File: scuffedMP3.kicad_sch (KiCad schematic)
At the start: 10 parts, among them J1 OLED, J2 Micro_SD_Card, J3 AudioJack3, U1 ESP32-WROVER-E, U2 TP4056-42-ESOP8, U3 CP2102N-Axx-xQFN24, U4 MCP1825S, U5 PCM5102A

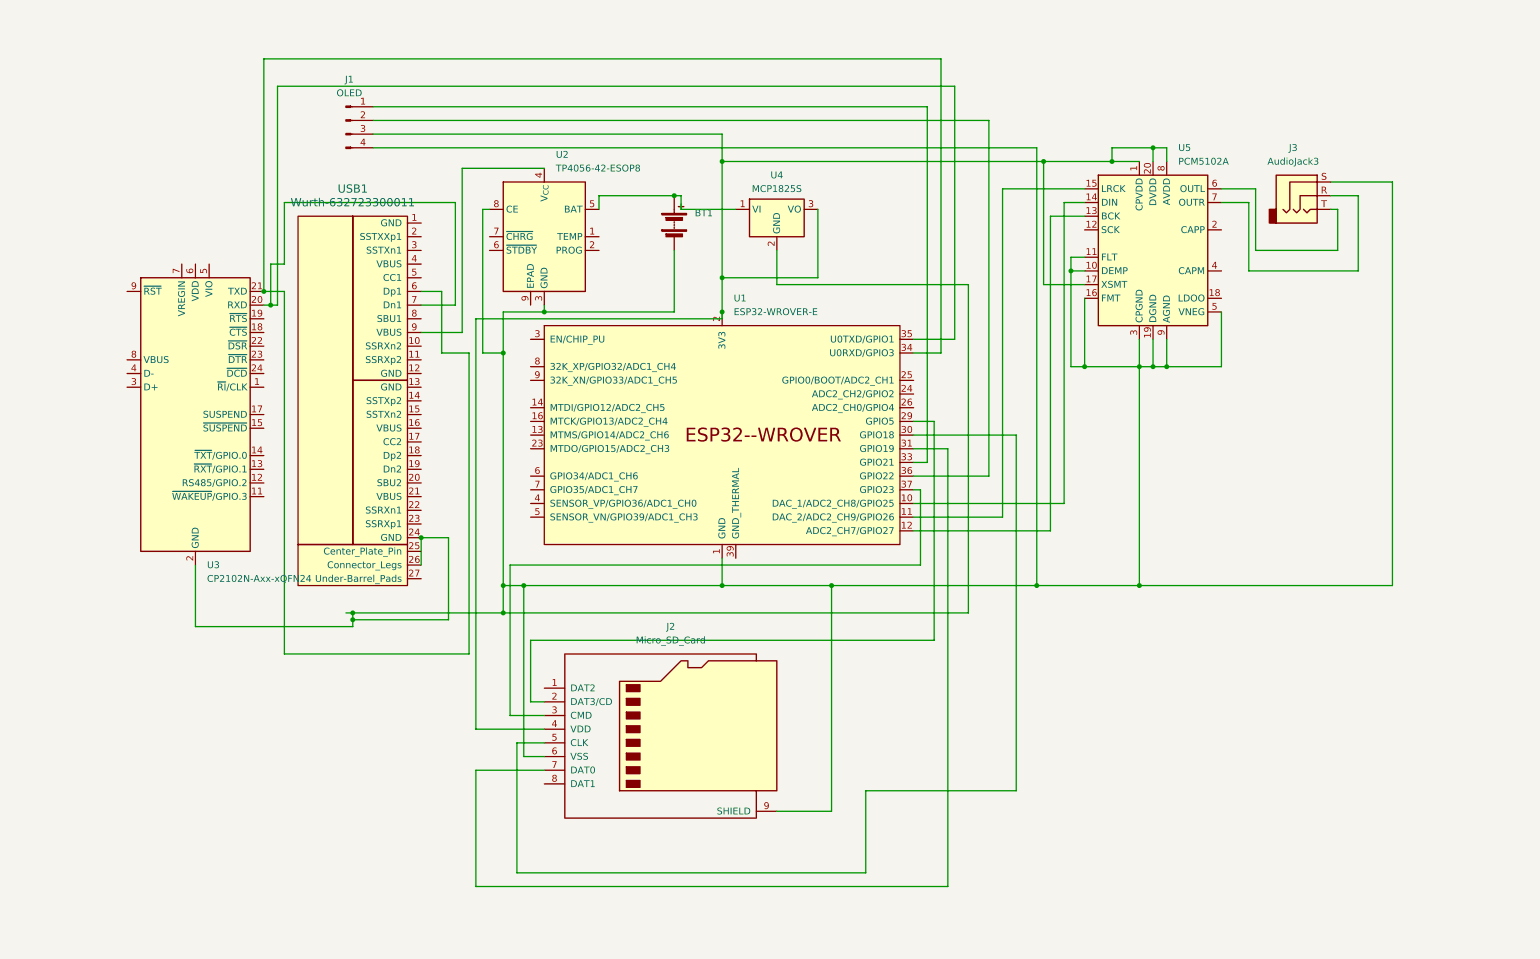
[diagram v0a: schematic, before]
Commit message: add touch sensor and wheel
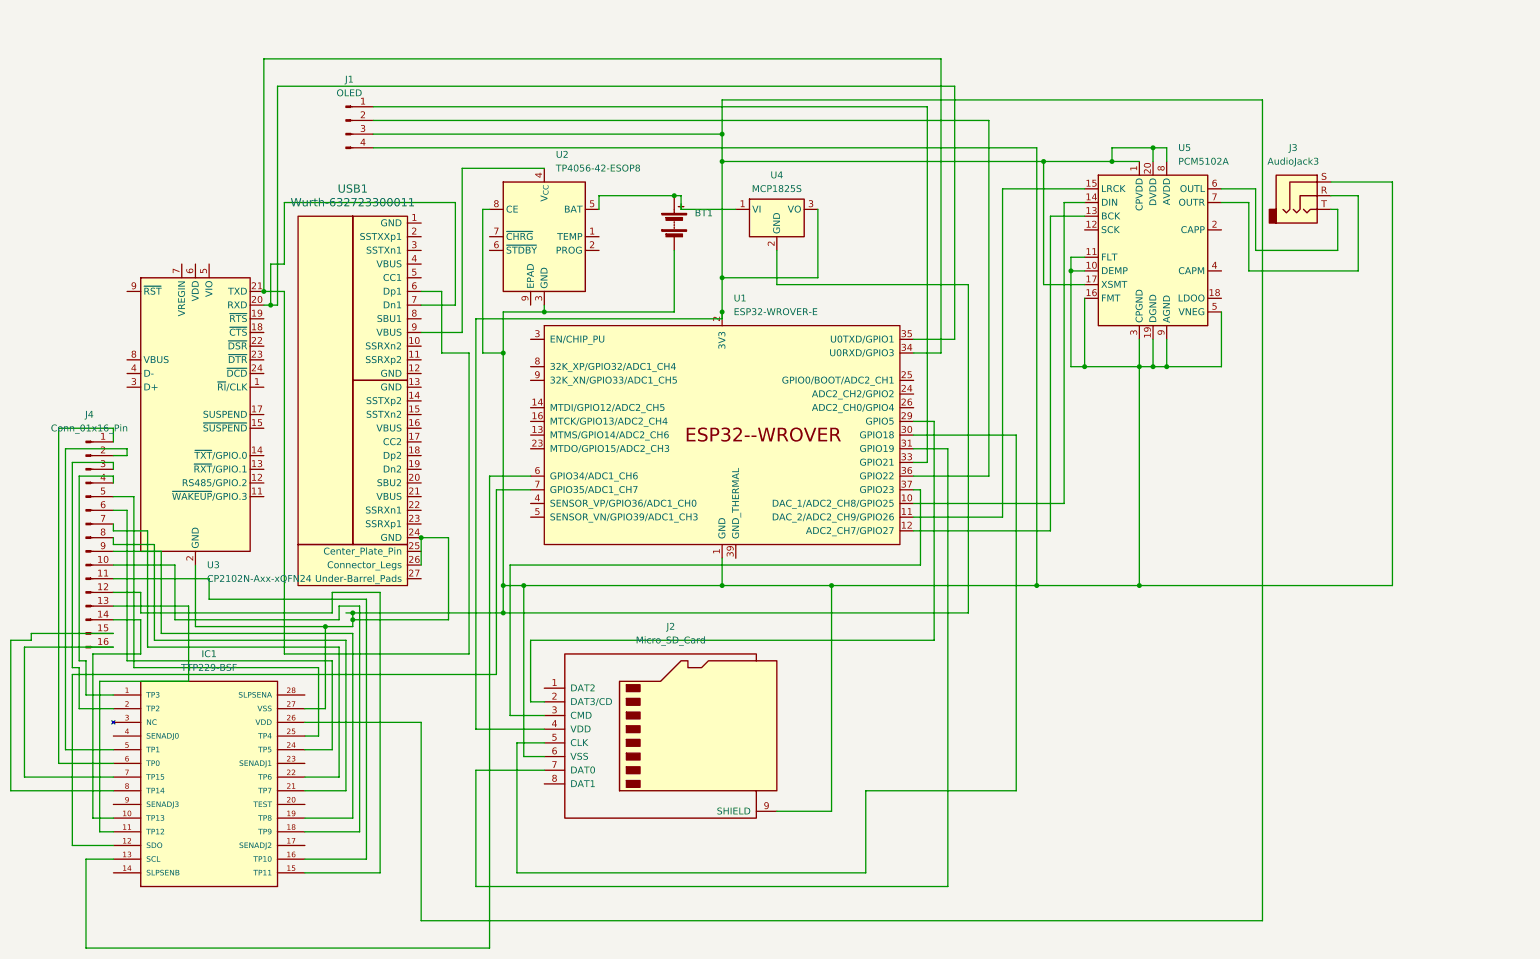
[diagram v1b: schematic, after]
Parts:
- added IC1: TTP229-BSF, TTP229-BSF:SOP64P600X175-28N, symbol TTP229-BSF:TTP229-BSF
- added J4: Conn_01x16_Pin, Library:ScrollWheel-40x12mm, symbol Connector:Conn_01x16_Pin
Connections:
- net at BT1.2 (-), J1.4 (Pin_4), J2.6 (VSS)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: now also IC1.27 (VSS)
- net at J1.3 (Pin_3), J2.4 (VDD), U1.2 (3V3)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: now also IC1.26 (VDD)
- net at U1.6 (GPIO34/ADC1_CH6): now also IC1.13 (SCL)
- net at U1.7 (GPIO35/ADC1_CH7): now also IC1.12 (SDO)
- new net: IC1.6 (TP0), J4.1 (Pin_1)
- new net: IC1.18 (TP9), J4.10 (Pin_10)
- new net: IC1.16 (TP10), J4.11 (Pin_11)
- new net: IC1.15 (TP11), J4.12 (Pin_12)
- new net: IC1.11 (TP12), J4.13 (Pin_13)
- new net: IC1.10 (TP13), J4.14 (Pin_14)
- new net: IC1.8 (TP14), J4.15 (Pin_15)
- new net: IC1.7 (TP15), J4.16 (Pin_16)
- new net: IC1.5 (TP1), J4.2 (Pin_2)
- new net: IC1.2 (TP2), J4.3 (Pin_3)
- new net: IC1.1 (TP3), J4.4 (Pin_4)
- new net: IC1.25 (TP4), J4.5 (Pin_5)
- new net: IC1.24 (TP5), J4.6 (Pin_6)
- new net: IC1.22 (TP6), J4.7 (Pin_7)
- new net: IC1.21 (TP7), J4.8 (Pin_8)
- new net: IC1.19 (TP8), J4.9 (Pin_9)

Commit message: progress
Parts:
- removed BT1: Battery, Connector_JST:JST_PH_S2B-PH-K_1x02_P2.00mm_Horizontal, symbol Device:Battery
- removed J1: OLED, OLED:128x64OLED, symbol Connector:Conn_01x04_Pin
- removed J2: Micro_SD_Card, Connector_Card:SD_Card_Device_16mm_SlotDepth, symbol Connector:Micro_SD_Card
- added 10kΩ1: R, symbol Device:R
- added C1, C3: 1 µF, Capacitor_SMD:C_0603_1608Metric, symbol Device:C_Small_US
- added C10, C8, C9: 1 µF, symbol Device:C_Small_US
- added C11: 0.1uF, symbol Device:C_Small_US
- added C2, C4: 0.1 µF, symbol Device:C_Small_US
- added C5, C6, C7: 0.1µF, symbol Device:C_Small_US
- added J2: DM3AT-SF-PEJM5, DM3AT-SF-PEJM5:HRS_DM3AT-SF-PEJM5, symbol DM3AT-SF-PEJM5:DM3AT-SF-PEJM5
- added R1: 10kΩ, symbol Device:R
- added U6: HS24S010B, easyeda2kicad:LCD-TH_L72.3-W43.0_HS24S010B, symbol OLED:HS24S010B
- J4: footprint Library:ScrollWheel-40x12mm -> Wheel:ScrollWheel-40x20mm
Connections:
- net GND: now reaches J3.S, U1.1 (GND), U1.15 (GND), U1.38 (GND), U2.3 (GND), U3.2 (GND), U3.25 (GND), U4.2 (GND), U5.16 (FMT), U5.19 (DGND), U5.3 (CPGND), U5.9 (AGND)
- net GND: now also U5.17 (XSMT), C1.2, C10.2, C11.1, C3.2, C5.1, C6.1, C7.1, C8.2, C9.2, U6.1 (GND); no longer IC1.27 (VSS), U2.8 (CE), U5.10 (DEMP), U5.11 (FLT), U5.5 (VNEG), USB1.24 (GND), USB1.26 (Connector_Legs)
- net at USB1.9 (VBUS): no longer U2.4 (V_{CC})
- net at J4.1 (Pin_1): no longer IC1.6 (TP0)
- net at J4.10 (Pin_10): no longer IC1.18 (TP9)
- net at J4.11 (Pin_11): no longer IC1.16 (TP10)
- net at J4.12 (Pin_12): no longer IC1.15 (TP11)
- net at J4.13 (Pin_13): no longer IC1.11 (TP12)
- net at J4.14 (Pin_14): no longer IC1.10 (TP13)
- net at J4.15 (Pin_15): no longer IC1.8 (TP14)
- net at J4.16 (Pin_16): no longer IC1.7 (TP15)
- net at J4.2 (Pin_2): no longer IC1.5 (TP1)
- net at J4.3 (Pin_3): no longer IC1.2 (TP2)
- net at J4.4 (Pin_4): no longer IC1.1 (TP3)
- net at J4.5 (Pin_5): no longer IC1.25 (TP4)
- net at J4.6 (Pin_6): no longer IC1.24 (TP5)
- net at J4.7 (Pin_7): no longer IC1.22 (TP6)
- net at J4.8 (Pin_8): no longer IC1.21 (TP7)
- net at J4.9 (Pin_9): no longer IC1.19 (TP8)
- net DAC DIN: now reaches U5.14 (DIN)
- net DAC DIN: now also U1.36 (GPIO22); no longer U1.10 (DAC_1/ADC2_CH8/GPIO25)
- net Bit Clock: now reaches U1.11 (DAC_2/ADC2_CH9/GPIO26)
- net Bit Clock: now also U5.13 (BCK); no longer U5.15 (LRCK)
- net OLED DC: now reaches U1.12 (ADC2_CH7/GPIO27)
- net OLED DC: now also U6.6 (DC); no longer U5.13 (BCK)
- net +3V3: now reaches U1.2 (3V3), U4.3 (VO), U5.1 (CPVDD), U5.20 (DVDD), U5.8 (AVDD)
- net +3V3: now also U3.6 (VDD), 10kΩ1.2, C1.1, C11.2, C5.2, C6.2, C7.2, R1.1, U6.2 (VCC); no longer IC1.26 (VDD), U5.17 (XSMT)
- net BOOT_SEL: now reaches U1.25 (GPIO0/BOOT/ADC2_CH1)
- net BOOT_SEL: now also 10kΩ1.1, C4.2
- net OLED CS: now reaches U1.29 (GPIO5)
- net OLED CS: now also U6.7 (CS)
- net EN: now reaches U1.3 (EN/CHIP_PU)
- net EN: now also C2.1, R1.2
- net OLED SCL: now reaches U1.30 (GPIO18)
- net OLED SCL: now also U6.3 (SCL)
- net OLED RST: now reaches U1.31 (GPIO19)
- net OLED RST: now also U6.11 (RST)
- net OLED LED: now reaches U1.33 (GPIO21)
- net OLED LED: now also U6.8 (LED)
- net MOSI OLED: now reaches U1.37 (GPIO23)
- net MOSI OLED: now also U6.4 (SDA)
- net at U1.6 (GPIO34/ADC1_CH6): no longer IC1.13 (SCL)
- net at U1.7 (GPIO35/ADC1_CH7): no longer IC1.12 (SDO)
- net at U5.2 (CAPP): now also C10.1
- net at U5.4 (CAPM): now also C8.1
- net BAT: now reaches U2.5 (BAT)
- net BAT: no longer U4.1 (VI)
- net at U3.19 (~{RTS}): now also C4.1
- net at U3.23 (~{DTR}): now also C2.2
- net USB_DP: now reaches U3.3 (D+)
- net USB_DM: now reaches U3.4 (D-)
- net VBUS: now reaches U3.7 (VREGIN)
- net VBUS: now also U2.4 (V_{CC}), U2.8 (CE), U3.8 (VBUS), U4.1 (VI), C3.1
- new net: C9.1, U5.5 (VNEG)
- new net: J2.P1 (SHIELD), J2.P2 (SHIELD), J2.P3 (SHIELD), J2.P4 (SHIELD)
- new net LR CLOCK: U1.10 (DAC_1/ADC2_CH8/GPIO25), U5.15 (LRCK)
- new net UART_RXD: U1.34 (U0RXD/GPIO3), U3.20 (RXD)
- new net UART_TXD: U1.35 (U0TXD/GPIO1), U3.21 (TXD)
- now unconnected: USB1.6 (Dp1), USB1.7 (Dn1)
- no-connect marks 0 -> 28
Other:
- moved on the sheet: J3, J4, U1, U2, U3, U4, U5, USB1

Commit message: upd
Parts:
- added C12, C13, C17, C18: 0.1 µF, Capacitor_SMD:C_0603_1608Metric, symbol Device:C_Small_US
- added C14, C15, C16: 1 µF, Capacitor_SMD:C_0603_1608Metric, symbol Device:C_Small_US
- added J1: battery, PHR-2:JST_PHR-2, symbol Connector_Generic:Conn_01x02
- added R2: 1.2 kΩ, Resistor_SMD:R_0603_1608Metric, symbol Device:R
- added R3, R4: 10 kΩ, Resistor_SMD:R_0603_1608Metric, symbol Device:R
- added R5, R6: 5.1 kΩ, Resistor_SMD:R_0603_1608Metric, symbol Device:R
- added SW1: SW_SPST, Button_Switch_SMD:SW_DIP_SPSTx01_Slide_6.7x4.1mm_W6.73mm_P2.54mm_LowProfile_JPin, symbol Switch:SW_SPST
- 10kΩ1, R1: footprint (none) -> Resistor_SMD:R_0603_1608Metric
- C10, C11, C2, C4, C5, C6, C7, C8, C9: footprint (none) -> Capacitor_SMD:C_0603_1608Metric
- J2: footprint DM3AT-SF-PEJM5:HRS_DM3AT-SF-PEJM5 -> micro_sd:HRS_DM3AT-SF-PEJM5
- J4: footprint Wheel:ScrollWheel-40x20mm -> Wheel:ScrollWheel-60x35mm
- U6: footprint easyeda2kicad:LCD-TH_L72.3-W43.0_HS24S010B -> OLED:LCD-TH_L72.3-W43.0_HS24S010B
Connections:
- net +3V3: now also IC1.26 (VDD), IC1.9 (SENADJ3), J2.4 (VDD), C12.1, C13.1, C17.1, C18.2, R3.2, R4.2, SW1.2 (B); no longer C1.1, U4.3 (VO)
- net BAT: now also C14.2, J1.1 (Pin_1)
- net GND: now also IC1.14 (SLPSENB), IC1.17 (SENADJ2), IC1.20 (TEST), IC1.23 (SENADJ1), IC1.27 (VSS), IC1.4 (SENADJ0), J2.6 (VSS), J2.P1 (SHIELD), J2.P2 (SHIELD), J2.P3 (SHIELD), J2.P4 (SHIELD), USB1.1 (GND), USB1.12 (GND), USB1.13 (GND), USB1.24 (GND), USB1.25 (Center_Plate_Pin), USB1.26 (Connector_Legs), USB1.27 (Under-Barrel_Pads), C12.2, C13.2, C14.1, C15.2, C16.1, C17.2, C18.1, J1.2 (Pin_2), R2.2, R5.2, R6.2
- net VBUS: now also USB1.16 (VBUS), USB1.21 (VBUS), USB1.4 (VBUS), USB1.9 (VBUS), C15.1, C16.2
- net at USB1.17 (CC2): now also R6.1
- net at USB1.5 (CC1): now also R5.1
- net TOUCH TP0: now reaches J4.1 (Pin_1)
- net TOUCH TP0: now also IC1.6 (TP0)
- net TOUCH TP9: now reaches J4.10 (Pin_10)
- net TOUCH TP9: now also IC1.18 (TP9)
- net TOUCH TP10: now reaches J4.11 (Pin_11)
- net TOUCH TP10: now also IC1.16 (TP10)
- net TOUCH TP11: now reaches J4.12 (Pin_12)
- net TOUCH TP11: now also IC1.15 (TP11)
- net TOUCH TP12: now reaches J4.13 (Pin_13)
- net TOUCH TP12: now also IC1.11 (TP12)
- net TOUCH TP13: now reaches J4.14 (Pin_14)
- net TOUCH TP13: now also IC1.10 (TP13)
- net TOUCH TP14: now reaches J4.15 (Pin_15)
- net TOUCH TP14: now also IC1.8 (TP14)
- net TOUCH TP15: now reaches J4.16 (Pin_16)
- net TOUCH TP15: now also IC1.7 (TP15)
- net TOUCH TP1: now reaches J4.2 (Pin_2)
- net TOUCH TP1: now also IC1.5 (TP1)
- net TOUCH TP2: now reaches J4.3 (Pin_3)
- net TOUCH TP2: now also IC1.2 (TP2)
- net TOUCH TP3: now reaches J4.4 (Pin_4)
- net TOUCH TP3: now also IC1.1 (TP3)
- net TOUCH TP4: now reaches J4.5 (Pin_5)
- net TOUCH TP4: now also IC1.25 (TP4)
- net TOUCH TP5: now reaches J4.6 (Pin_6)
- net TOUCH TP5: now also IC1.24 (TP5)
- net TOUCH TP6: now reaches J4.7 (Pin_7)
- net TOUCH TP6: now also IC1.22 (TP6)
- net TOUCH TP7: now reaches J4.8 (Pin_8)
- net TOUCH TP7: now also IC1.21 (TP7)
- net TOUCH TP8: now reaches J4.9 (Pin_9)
- net TOUCH TP8: now also IC1.19 (TP8)
- net MICRO CD: now reaches J2.2 (CD/DAT3)
- net MICRO CMD: now reaches J2.3 (CMD)
- net MICRO CMD: now also U1.26 (ADC2_CH0/GPIO4)
- net MICRO CLK: now reaches J2.5 (CLK)
- net MICRO CLK: now also U1.24 (ADC2_CH2/GPIO2)
- net MICRO DAT0: now reaches J2.7 (DAT0)
- net MICRO DAT0: now also U1.8 (32K_XP/GPIO32/ADC1_CH4)
- net TOUCH SCL: now reaches U1.9 (32K_XN/GPIO33/ADC1_CH5)
- net TOUCH SCL: now also IC1.13 (SCL)
- net at U2.2 (PROG): now also R2.1
- net TOUCH SDO: now reaches IC1.12 (SDO)
- net at IC1.28 (SLPSENA): now also R4.1
- net at U3.9 (~{RST}): now also R3.1
- new net 3V3 IN: C1.1, SW1.1 (A), U4.3 (VO)
- no-connect marks 28 -> 30
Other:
- moved on the sheet: C1, C3, J2, J4, U4
